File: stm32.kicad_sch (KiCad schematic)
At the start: 9 parts, among them CN2 XY308-2.54-4P, CN3 SM04B-SRSS-TB (LF)(SN), CN4 SM04B-SRSS-TB (LF)(SN), U1 STM32G431CBT6, U2 DRV8323SRTAR, U3 TMC2209-LA-T, U4 DRV8876PWPR, U6 HB-PH9-12727PB2GOB, U8 XY308-2.54-2P

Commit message: WIP
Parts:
- added C38, C49: CL10A475KO8NNNC, easyeda2kicad:C0603, symbol easyeda2kicad:CL10A475KO8NNNC
- added C39, C40, C41, C46, C47, C50, C51, C52, C53: CC0603KRX7R9BB104, easyeda2kicad:C0603, symbol easyeda2kicad:CC0603KRX7R9BB104
- added C42, C43, C48: CL10A105KB8NNNC, easyeda2kicad:C0603, symbol easyeda2kicad:CL10A105KB8NNNC
- added C44, C45: 0603CG7R0C500NT, easyeda2kicad:C0603, symbol easyeda2kicad:0603CG7R0C500NT
- added R20, R34, R40: 0603WAF4701T5E, easyeda2kicad:R0603, symbol easyeda2kicad:0603WAF4701T5E
- added R21, R30, R31: 0603WAF1002T5E, easyeda2kicad:R0603, symbol easyeda2kicad:0603WAF1002T5E
- added R28, R29: 0603WAF0000T5E, easyeda2kicad:R0603, symbol easyeda2kicad:0603WAF0000T5E
- added R41: 0603WAF1001T5E, easyeda2kicad:R0603, symbol easyeda2kicad:0603WAF1001T5E
- added R42: 0603WAF1000T5E, easyeda2kicad:R0603, symbol easyeda2kicad:0603WAF1000T5E
- added SW2: 6.0*6.0*6.0, easyeda2kicad:SW-SMD_4P-L6.0-W6.0-P4.50-LS8.6, symbol easyeda2kicad:6.0*6.0*6.0
- added X1: SC-32S32.768kHz20PPM7pF, easyeda2kicad:OSC-SMD_L3.2-W1.5, symbol easyeda2kicad:SC-32S32.768kHz20PPM7pF
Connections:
- net +3V3: now reaches U1.1 (VBAT)
- net +3V3: now also U1.20 (VREF+), U1.21 (VDDA), U1.24 (VDD), U1.36 (VDD), U1.48 (VDD), U3.15 (VCC_IO), U6.3, C38.1, C39.1, C40.1, C41.1, C42.1, C43.1, C46.1, C47.1, C48.1, C50.1, R20.1, R30.2, R31.2, R34.1, R40.1
- net GND: now reaches U1.19 (VSSA)
- net GND: now also U1.23 (VSS), U1.35 (VSS), U1.47 (VSS), U3.18 (GND), U3.20 (STDBY), U3.29 (EP), U3.3 (GND), U6.5, U6.7, C38.2, C39.2, C40.2, C41.2, C42.2, C43.2, C44.1, C45.1, C46.2, C47.2, C48.2, C49.2, C50.2, C51.2, C52.2, R21.1, R42.2, SW2.3, SW2.4
- net at U1.3 (PC14-OSC32_IN): now also R28.2
- net SWDIO: now reaches U1.37 (PA13)
- net SWDIO: now also U6.4, R40.2
- net SWCLK: now reaches U1.38 (PA14)
- net SWCLK: now also U6.6, R34.2
- net at U1.4 (PC15-OSC32_OUT): now also R29.2
- net BOOT0: now reaches U1.45 (PB8-BOOT0)
- net BOOT0: now also R20.2, R21.2
- net STM32_NRST: now reaches U1.7 (PG10-NRST)
- net STM32_NRST: now also R30.1, SW2.1, SW2.2
- net at U6.11: now also R42.1
- net VCP_RX: now reaches U6.13
- net VCP_TX: now reaches U6.14
- net UART_PDN_RX: now reaches U3.14 (PDN_UART)
- net UART_PDN_RX: now also R41.2
- net STEPPER_EN: now reaches U3.2 (ENN)
- net STEPPER_EN: now also R31.1
- net +VBAT: now reaches U3.22 (VS)
- net +VBAT: now also U3.28 (VS), C51.1, C52.1, C53.1
- net at U3.6 (VCP): now also C53.2
- net at U3.8 (5VOUT): now also C49.1
- new net OSC32_IN: C44.2, R28.1, X1.1
- new net OSC32_OUT: C45.2, R29.1, X1.2
- new net UART_PDN_TX: R41.1
- no-connect marks 5 -> 7
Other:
- note added: "ENN: enable=0 disable=1"
- note added: "JTAG/SW CONN"
- note added: "Original part number for the stm32 v3 set is : FTSH-107-01-L-DV-K-A"
- note added: "PB_SWITCH"
- note added: "VBAT"
- note added: "VDD"
- note added: "VDDA"
- note added: "VREF"
- moved on the sheet: CN2, U2, U3, U4, U8

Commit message: stepper and dc motors and stm32 config pins are ready
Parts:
- removed C42, C43, C48: CL10A105KB8NNNC, easyeda2kicad:C0603, symbol easyeda2kicad:CL10A105KB8NNNC
- removed C44, C45: 0603CG7R0C500NT, easyeda2kicad:C0603, symbol easyeda2kicad:0603CG7R0C500NT
- removed R20: 0603WAF4701T5E, easyeda2kicad:R0603, symbol easyeda2kicad:0603WAF4701T5E
- removed R28, R29: 0603WAF0000T5E, easyeda2kicad:R0603, symbol easyeda2kicad:0603WAF0000T5E
- removed X1: SC-32S32.768kHz20PPM7pF, easyeda2kicad:OSC-SMD_L3.2-W1.5, symbol easyeda2kicad:SC-32S32.768kHz20PPM7pF
- added C1, C10, C2, C3, C4: CL10B105KA8NNNC, easyeda2kicad:C0603, symbol easyeda2kicad:CL10B105KA8NNNC
- added C54, C55: CC0603KRX7R9BB104, easyeda2kicad:C0603, symbol easyeda2kicad:CC0603KRX7R9BB104
- added C56: ~, easyeda2kicad:C0603, symbol easyeda2kicad:CC0603KRX7R9BB104
- added C9: CL21A226MAYNNNE, easyeda2kicad:C0805, symbol easyeda_symbole:CL21A226MAYNNNE
- added D10, D11, D12: KT-0603R, easyeda2kicad:LED0603-RD, symbol easyeda2kicad:KT-0603R
- added D3: 0603 Green 509-620mcd, easyeda2kicad:LED0603-RD, symbol easyeda2kicad:0603Green509-620mcd
- added R22: ~, easyeda2kicad:R0603, symbol easyeda2kicad:0603WAF1002T5E
- added R23, R24, R25, R26: 0603WAF1000T5E, easyeda2kicad:R0603, symbol easyeda2kicad:0603WAF1000T5E
- added R32: 0603WAF1002T5E, easyeda2kicad:R0603, symbol easyeda2kicad:0603WAF1002T5E
- added R4, R6: 0603WAF1003T5E, easyeda2kicad:R0603, symbol easyeda2kicad:0603WAF1003T5E
- added R5: 0603WAF0000T5E, easyeda2kicad:R0603, symbol easyeda2kicad:0603WAF0000T5E
- added SW3: 6.0*6.0*6.0, easyeda2kicad:SW-SMD_4P-L6.0-W6.0-P4.50-LS8.6, symbol easyeda2kicad:6.0*6.0*6.0
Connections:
- net +3V3: now also U4.5 (VREF), C2.1, C3.1, C4.1, R26.1, R32.2
- net +VBAT: now also U4.11 (VM), C1.1, C10.1, C54.1, C55.2
- net GND: now also U3.2 (ENN), U3.23 (BRA), U3.25 (UNUSED), U3.27 (BRB), U4.15 (GND), U4.16 (PMODE), U4.17 (EP), U4.6 (IPROPI), U4.7 (IMODE), U4.9 (PGND), C1.2, C10.2, C2.2, C3.2, C4.2, C54.2, D10.1 (K), D11.1 (K), D3.1 (K), R22.1, R4.1, R5.2, SW3.3, SW3.4; no longer U3.20 (STDBY)
- net UART_PDN_RX: now also R22.2
- net at C49.1, U3.8 (5VOUT): now also R6.2
- net at U8.1: now also U4.8 (OUT1)
- net at U8.2: now also U4.10 (OUT2)
- net OSC_IN: now reaches U1.5 (PF0-OSC_IN)
- net OSC_OUT: now reaches U1.6 (PF1-OSC_OUT)
- net STEPPER_DIAG: now reaches U3.11 (DIAG)
- net STEPPER_DIAG: now also R25.2
- net at U3.13 (CLK): now also R5.1
- net STEPPER_STEP: now reaches U3.16 (STEP)
- net at U3.17 (VREF): now also R6.1
- net STEPPER_DIR: now reaches U3.19 (DIR)
- net at U3.4 (CPO): now also C9.1
- net at U3.5 (CPI): now also C9.2
- net DC_MOTOR_PWM_EN: now reaches U4.1 (EN/IN1)
- net at U4.12 (VCP): now also C55.1
- net at U4.13 (CPH): now also C56.2
- net at U4.14 (CPL): now also C56.1
- net DC_MOTOR_DIR: now reaches U4.2 (PH/IN2)
- net DC_MOTOR_SLEEP: now reaches U4.3 (nSLEEP)
- net LED_FAULT: now reaches U4.4 (nFAULT)
- net LED_FAULT: now also R31.1, D12.1 (K)
- net MOTOR_A1 renamed STEPPER_A1
- net MOTOR_A2 renamed STEPPER_A2
- net MOTOR_B1 renamed STEPPER_B1
- net MOTOR_B2 renamed STEPPER_B2
- removed net STEPPER_EN: R31.1, U3.2 (ENN)
- new net: D12.2 (A), R26.2
- new net: D3.2 (A), R23.1
- new net: D10.2 (A), R24.1
- new net: D11.2 (A), R25.1
- new net LED1: R23.2
- new net LED2: R24.2
- new net PB_SW1: R32.1, SW3.1, SW3.2
- new net STEPPER_STDBY: R4.2, U3.20 (STDBY)
- no-connect marks 7 -> 11
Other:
- note added: "I2C"
- note added: "LEDS"
- note added: "SPI"
- moved on the sheet: C38, C39, C40, C41, C46, C47, C49, CN3, R21, R34, R40, R41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

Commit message: bldc connections and stm32 io connection and adjustments
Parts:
- removed D10: KT-0603R, easyeda2kicad:LED0603-RD, symbol easyeda2kicad:KT-0603R
- removed R24: 0603WAF1000T5E, easyeda2kicad:R0603, symbol easyeda2kicad:0603WAF1000T5E
- added C12, C15: CL10B105KA8NNNC, easyeda2kicad:C0603, symbol easyeda2kicad:CL10B105KA8NNNC
- added C13, C14: ~, easyeda2kicad:C0603, symbol easyeda2kicad:CL10B105KA8NNNC
- added C59, C60: CC0603KRX7R9BB104, easyeda2kicad:C0603, symbol easyeda2kicad:CC0603KRX7R9BB104
- added D13: KT-0603R, easyeda2kicad:LED0603-RD, symbol easyeda2kicad:KT-0603R
- added R13, R16, R33, R35: 0603WAF1002T5E, easyeda2kicad:R0603, symbol easyeda2kicad:0603WAF1002T5E
- added R27: 0603WAF1000T5E, easyeda2kicad:R0603, symbol easyeda2kicad:0603WAF1000T5E
- added R28: 0603WAF220JT5E, easyeda2kicad:R0603, symbol easyeda2kicad:0603WAF220JT5E
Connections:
- net +3V3: now also CN4.2, U2.24 (VREF), C60.1, R13.2, R16.2, R27.1, R33.2, R35.2
- net +VBAT: now also U2.4 (VM), U2.5 (VDRAIN), C12.2, C13.2, C59.1
- net DC_MOTOR_DIR: now also U1.43 (PB6)
- net DC_MOTOR_PWM_EN: now also U1.31 (PA9)
- net DC_MOTOR_SLEEP: now also U1.2 (PC13)
- net GND: now also CN4.1, U2.32 (AGND), U2.40 (PGND), U2.41 (EP), C13.1, C15.1, C59.2, C60.2
- net LED1: now also U1.4 (PC15-OSC32_OUT)
- net PB_SW1: now also U1.3 (PC14-OSC32_IN)
- net STEPPER_DIR: now also U1.33 (PA11)
- net STEPPER_STDBY: now also U1.34 (PA12)
- net STEPPER_STEP: now also U1.32 (PA10)
- net VCP_RX: now also U1.11 (PA3)
- net VCP_TX: now also U1.10 (PA2)
- net BLDC_SPI_CS: now reaches U1.12 (PA4)
- net BLDC_SPI_CS: now also U2.29 (nSCS)
- net BLDC_SPI_SCK: now reaches U1.13 (PA5)
- net BLDC_SPI_SCK: now also U2.28 (SCLK)
- net BLDC_SPI_MISO: now reaches U1.14 (PA6)
- net BLDC_SPI_MISO: now also U2.26 (SDO), R33.1
- net BLDC_SPI_MOSI: now reaches U1.15 (PA7)
- net BLDC_SPI_MOSI: now also U2.27 (SDI)
- net VSENSE_C: now reaches U1.16 (PB0)
- net VSENSE_B: now reaches U1.17 (PB1)
- net VSENSE_A: now reaches U1.18 (PB2)
- net BLDC_STOP: now reaches U1.22 (PB10)
- net BLDC_STOP: now also U2.30 (ENABLE), U2.35 (INLA), U2.37 (INLB), U2.39 (INLC)
- net BLDC_SOC: now reaches U1.25 (PB11)
- net BLDC_SOC: now also U2.21 (SOC)
- net SPI2_CS: now reaches U1.26 (PB12)
- net SPI2_CS: now also CN3.1
- net SPI2_SCK: now reaches U1.27 (PB13)
- net SPI2_SCK: now also CN3.2
- net SPI2_MISO: now reaches U1.28 (PB14)
- net SPI2_MISO: now also CN3.3
- net SPI2_MOSI: now reaches U1.29 (PB15)
- net SPI2_MOSI: now also CN3.4
- net I2C3_SCL_R: now reaches U1.30 (PA8)
- net I2C3_SCL_R: now also R28.1
- net BLDC_INHC: now reaches U1.39 (PA15)
- net BLDC_INHC: now also U2.38 (INHC)
- net BLDC_INHB: now reaches U1.40 (PB3)
- net BLDC_INHB: now also U2.36 (INHB)
- net BLDC_INHA: now reaches U1.41 (PB4)
- net BLDC_INHA: now also U2.34 (INHA)
- net I2C3_SDA: now reaches U1.42 (PB5)
- net I2C3_SDA: now also CN4.3, R13.1
- net BLDC_SOA: now reaches U1.8 (PA0)
- net BLDC_SOA: now also U2.23 (SOA)
- net BLDC_SOB: now reaches U1.9 (PA1)
- net BLDC_SOB: now also U2.22 (SOB)
- net at U2.1 (CPL): now also C14.2
- net SNA: now reaches U2.10 (SNA)
- net SNB: now reaches U2.11 (SNB)
- net SPB: now reaches U2.12 (SPB)
- net GLB: now reaches U2.13 (GLB)
- net SHB: now reaches U2.14 (SHB)
- net GHB: now reaches U2.15 (GHB)
- net GHC: now reaches U2.16 (GHC)
- net SHC: now reaches U2.17 (SHC)
- net GLC: now reaches U2.18 (GLC)
- net SPC: now reaches U2.19 (SPC)
- net at U2.2 (CPH): now also C14.1
- net SNC: now reaches U2.20 (SNC)
- net BLDC_LED_FAULT: now reaches U2.25 (nFAULT)
- net BLDC_LED_FAULT: now also D13.1 (K), R35.1
- net at U2.3 (VCP): now also C12.1
- net 3V3_OUT: now reaches U2.33 (DVDD)
- net 3V3_OUT: now also C15.2
- net GHA: now reaches U2.6 (GHA)
- net SHA: now reaches U2.7 (SHA)
- net GLA: now reaches U2.8 (GLA)
- net SPA: now reaches U2.9 (SPA)
- net I2C3_SCL: now reaches CN4.4
- net I2C3_SCL: now also R16.1, R28.2
- net LED_FAULT renamed DC_MOTOR_LED_FAULT
- new net: D13.2 (A), R27.2
- no-connect marks 11 -> 15
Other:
- note added: "STM32G4"
- note removed: "stm32g4"
- moved on the sheet: C2, C3, C38, C39, C4, C40, C41, C46, C47, CN4, D12, D3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

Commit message: connection updates after lampel review
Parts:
- removed C9: CL21A226MAYNNNE, easyeda2kicad:C0805, symbol easyeda_symbole:CL21A226MAYNNNE
- removed R22: ~, easyeda2kicad:R0603, symbol easyeda2kicad:0603WAF1002T5E
- removed R31: 0603WAF1002T5E, easyeda2kicad:R0603, symbol easyeda2kicad:0603WAF1002T5E
- removed R4: 0603WAF1003T5E, easyeda2kicad:R0603, symbol easyeda2kicad:0603WAF1003T5E
- removed R5: 0603WAF0000T5E, easyeda2kicad:R0603, symbol easyeda2kicad:0603WAF0000T5E
- added C57: ~, easyeda2kicad:C0603, symbol easyeda2kicad:CC0603KRX7R9BB104
- added R36: 0603WAF1002T5E, easyeda2kicad:R0603, symbol easyeda2kicad:0603WAF1002T5E
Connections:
- net +3V3: now also R36.2
- net BLDC_LED_FAULT: now also U1.44 (PB7)
- net GND: now also U3.13 (CLK), U3.9 (MS1_AD0)
- net at U3.4 (CPO): now also C57.2
- net at U3.5 (CPI): now also C57.1
- net at U3.10 (MS2_AD1): now also R36.1
- no-connect marks 15 -> 13
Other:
- moved on the sheet: D11, D13, R25, R27, R41

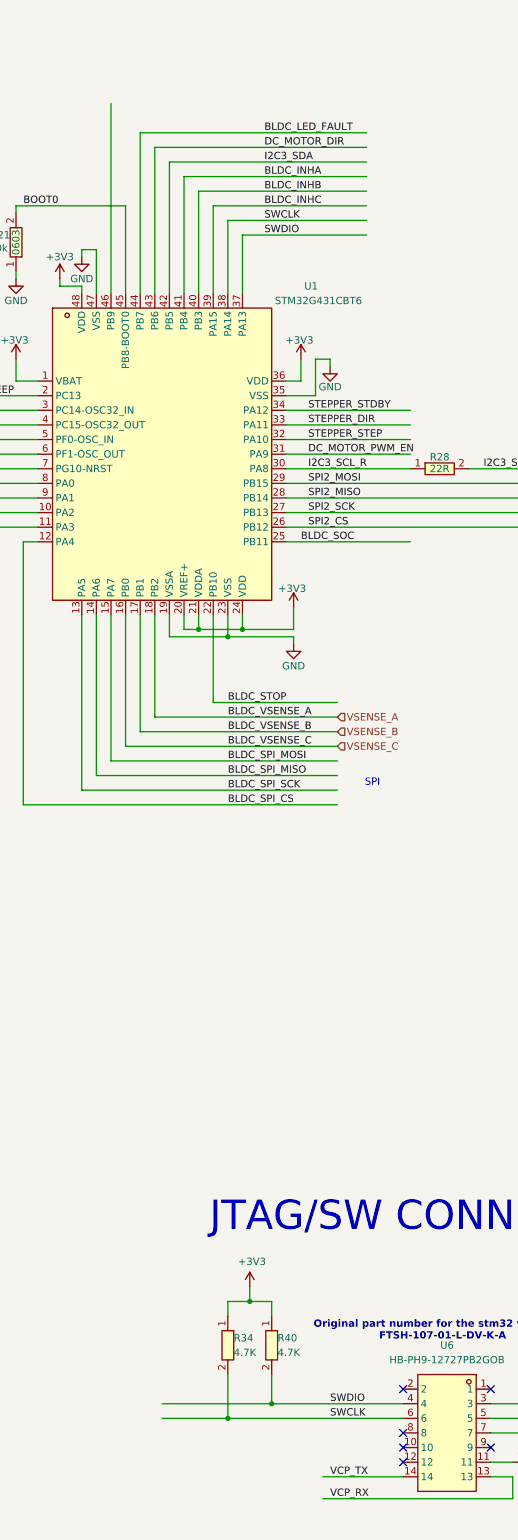
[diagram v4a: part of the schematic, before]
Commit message: adding SWO pin
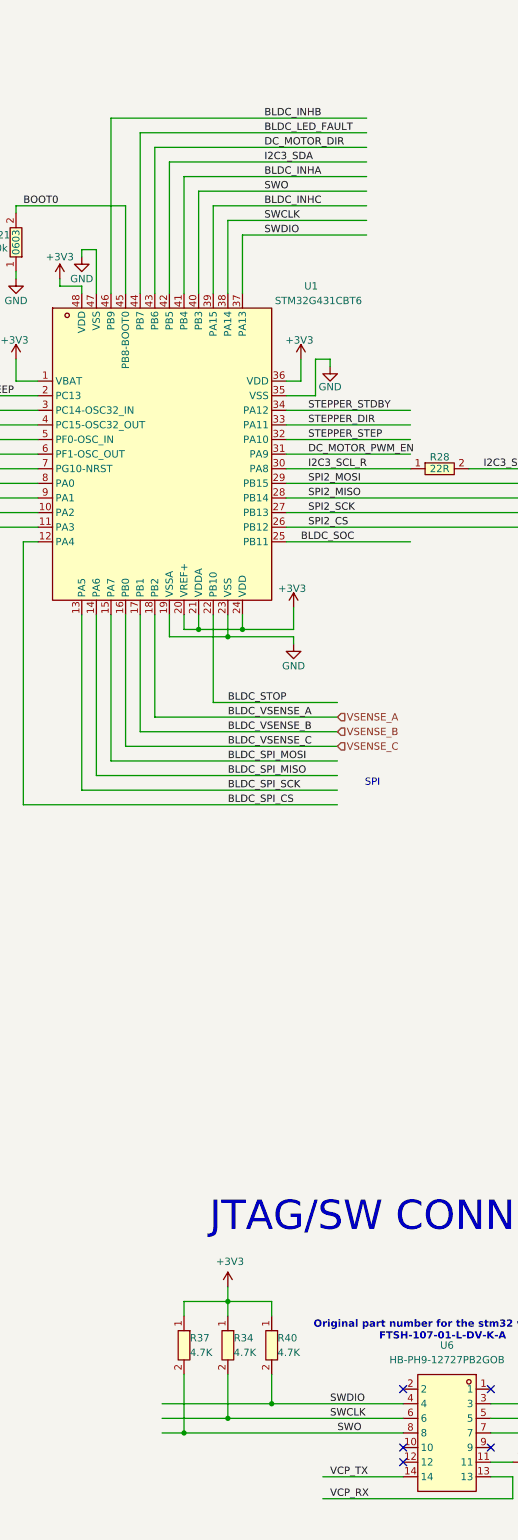
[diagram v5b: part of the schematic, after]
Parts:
- added R37: 0603WAF4701T5E, easyeda2kicad:R0603, symbol easyeda2kicad:0603WAF4701T5E
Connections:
- net +3V3: now also R37.1
- net BLDC_INHB: now also U1.46 (PB9); no longer U1.40 (PB3)
- net SWO: now reaches U6.8
- net SWO: now also U1.40 (PB3), R37.2
- no-connect marks 13 -> 12
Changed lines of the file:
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@@
 	)
 	(junction
+		(at 173.99 306.07)
+		(diameter 0)
+		(color 0 0 0 0)
+	)
+	(junction
 		(at 173.99 326.39)
 		(diameter 0)
@@
 	)
 	(junction
-		(at 177.8 306.07)
-		(diameter 0)
-		(color 0 0 0 0)
-	)
-	(junction
 		(at 502.92 52.07)
 		(diameter 0)
@@
 	)
 	(junction
+		(at 166.37 328.93)
+		(diameter 0)
+		(color 0 0 0 0)
+	)
+	(junction
 		(at 48.26 92.71)
 		(diameter 0)
@@
 	)
 	(no_connect
-		(at 204.47 328.93)
-	)
-	(no_connect
 		(at 204.47 321.31)
 	)
@@
 	(wire
 		(pts
+			(xy 166.37 318.77) (xy 166.37 328.93)
+		)
+		(stroke
+			(width 0)
+			(type default)
+		)
+	)
+	(wire
+		(pts
 			(xy 184.15 151.13) (xy 205.74 151.13)
 		)
@@
 	(wire
 		(pts
+			(xy 153.67 100.33) (xy 198.12 100.33)
+		)
+		(stroke
+			(width 0)
+			(type default)
+		)
+	)
+	(wire
+		(pts
 			(xy 163.83 107.95) (xy 198.12 107.95)
 		)
@@
 	(wire
 		(pts
+			(xy 166.37 328.93) (xy 204.47 328.93)
+		)
+		(stroke
+			(width 0)
+			(type default)
+		)
+	)
+	(wire
+		(pts
 			(xy 501.65 162.56) (xy 492.76 162.56)
 		)
@@
 	(wire
 		(pts
-			(xy 153.67 97.79) (xy 153.67 130.81)
+			(xy 153.67 100.33) (xy 153.67 130.81)
 		)
 		(stroke
 			(width 0)
 			(type default)
-			(color 255 0 0 1)
 		)
 	)
@@
 	(wire
 		(pts
+			(xy 166.37 306.07) (xy 173.99 306.07)
+		)
+		(stroke
+			(width 0)
+			(type default)
+		)
+	)
+	(wire
+		(pts
 			(xy 118.11 171.45) (xy 140.97 171.45)
 		)
@@
 	(wire
 		(pts
+			(xy 166.37 308.61) (xy 166.37 306.07)
+		)
+		(stroke
+			(width 0)
+			(type default)
+		)
+	)
+	(wire
+		(pts
 			(xy 414.02 222.25) (xy 414.02 208.28)
 		)
@@
 	(wire
 		(pts
+			(xy 162.56 328.93) (xy 166.37 328.93)
+		)
+		(stroke
+			(width 0)
+			(type default)
+		)
+	)
+	(wire
+		(pts
 			(xy 184.15 168.91) (xy 267.97 168.91)
 		)
@@
 	(wire
 		(pts
-			(xy 181.61 306.07) (xy 177.8 306.07)
-		)
-		(stroke
-			(width 0)
-			(type default)
-		)
-	)
-	(wire
-		(pts
 			(xy 236.22 328.93) (xy 236.22 334.01)
 		)
@@
 	(wire
 		(pts
-			(xy 177.8 306.07) (xy 173.99 306.07)
+			(xy 173.99 306.07) (xy 181.61 306.07)
 		)
 		(stroke
@@
 	(wire
 		(pts
-			(xy 177.8 306.07) (xy 177.8 303.53)
+			(xy 173.99 306.07) (xy 173.99 303.53)
 		)
 		(stroke
@@
 		)
 	)
-	(label "BLDC_INHB"
-		(at 180.34 113.03 0)
-		(effects
-			(font
-				(size 1.27 1.27)
-			)
-			(justify left bottom)
-		)
-	)
 	(label "STEPPER_A2"
 		(at 500.38 72.39 0)
@@
 		)
 	)
+	(label "SWO"
+		(at 180.34 113.03 0)
+		(effects
+			(font
+				(size 1.27 1.27)
+			)
+			(justify left bottom)
+		)
+	)
 	(label "VCP_RX"
 		(at 191.77 340.36 0)
@@
 		)
 	)
+	(label "SWO"
+		(at 193.04 328.93 0)
+		(effects
+			(font
+				(size 1.27 1.27)
+			)
+			(justify left bottom)
+		)
+	)
 	(label "BLDC_SPI_MISO"
 		(at 438.15 205.74 0)
@@
 		)
 	)
+	(label "BLDC_INHB"
+		(at 180.34 100.33 0)
+		(effects
+			(font
+				(size 1.27 1.27)
+			)
+			(justify left bottom)
+		)
+	)
 	(label "I2C3_SCL"
 		(at 218.44 161.29 0)
@@
 	(symbol
 		(lib_id "SAMC21_breakout-rescue:+3V3-power")
-		(at 177.8 303.53 0)
+		(at 173.99 303.53 0)
 		(unit 1)
 		(exclude_from_sim no)
@@
 		(dnp no)
 		(property "Reference" "#PWR021"
-			(at 177.8 307.34 0)
+			(at 173.99 307.34 0)
 			(effects
 				(font
@@
 		)
 		(property "Value" "+3V3"
-			(at 178.181 299.1358 0)
+			(at 174.371 299.1358 0)
 			(effects
 				(font
@@
 		)
 		(property "Footprint" ""
-			(at 177.8 303.53 0)
+			(at 173.99 303.53 0)
 			(effects
 				(font
@@
 		)
 		(property "Datasheet" ""
-			(at 177.8 303.53 0)
+			(at 173.99 303.53 0)
 			(effects
 				(font
@@
 		)
 		(property "Description" ""
-			(at 177.8 303.53 0)
+			(at 173.99 303.53 0)
 			(effects
 				(font
@@
 					(unit 1)
 				)
+			)
+		)
+	)
+	(symbol
+		(lib_id "easyeda2kicad:0603WAF4701T5E")
+		(at 166.37 313.69 270)
+		(unit 1)
+		(exclude_from_sim no)
+		(in_bom yes)
+		(on_board yes)
+		(dnp no)
+		(property "Reference" "R37"
+			(at 167.386 312.42 90)
+			(effects
+				(font
+					(size 1.27 1.27)
+				)
+				(justify left)
+			)
+		)
+		(property "Value" "0603WAF4701T5E"
+			(at 161.29 313.69 0)
+			(effects
+				(font
+					(size 1.27 1.27)
+				)
+				(hide yes)
+			)
+		)
+		(property "Footprint" "easyeda2kicad:R0603"
+			(at 158.75 313.69 0)
+			(effects
+				(font
+					(size 1.27 1.27)
+				)
+				(hide yes)
+			)
+		)
+		(property "Datasheet" "https://lcsc.com/product-detail/Chip-Resistor-Surface-Mount-UniOhm_4-7KR-4701-1_C23162.html"
+			(at 156.21 313.69 0)
+			(effects
+				(font
+					(size 1.27 1.27)
+				)
+				(hide yes)
+			)
+		)
+		(property "Description" "4.7K"
+			(at 167.386 314.96 90)
+			(effects
+				(font
+					(size 1.27 1.27)
+				)
+				(justify left)
+			)
+		)
+		(property "LCSC Part" "C23162"
+			(at 153.67 313.69 0)
+			(effects
+				(font
+					(size 1.27 1.27)
+				)
+				(hide yes)
+			)
+		)
+		(pin "1"
+		)
+		(pin "2"
+		)
+		(instances
+			(project "stm32G4"
+				(path "/97277ecc-4d45-42d3-be9a-6b43805ad0c6/9223e125-7c28-4305-a4e4-f70e2a17a8a2"
+					(reference "R37")
+					(unit 1)
+				)

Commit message: Added swaps
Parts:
- added C11, C9: CL10C150JB8NNNC, easyeda2kicad:C0603, symbol easyeda_symbole:CL10C150JB8NNNC
- added R4: 0603WAF1001T5E, easyeda2kicad:R0603, symbol easyeda_symbole:0603WAF1001T5E
- added U5: ABM8-272-T3_C20625731, easyeda2kicad:CRYSTAL-SMD_4P-L3.2-W2.5-BL, symbol easyeda_symbole:ABM8-272-T3_C20625731
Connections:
- net BLDC_INHA: now also U1.30 (PA8); no longer U1.41 (PB4)
- net BLDC_INHB: now also U1.31 (PA9); no longer U1.46 (PB9)
- net BLDC_INHC: now also U1.32 (PA10); no longer U1.39 (PA15)
- net BLDC_LED_FAULT: now also U1.17 (PB1); no longer U1.44 (PB7)
- net BLDC_SOA: now also U1.10 (PA2); no longer U1.8 (PA0)
- net BLDC_SOB: now also U1.12 (PA4); no longer U1.9 (PA1)
- net BLDC_SOC: now also U1.11 (PA3); no longer U1.25 (PB11)
- net BLDC_SPI_CS: now also U1.16 (PB0); no longer U1.12 (PA4)
- net BLDC_STOP: now also U1.34 (PA12); no longer U1.22 (PB10)
- net DC_MOTOR_DIR: now also U1.2 (PC13); no longer U1.43 (PB6)
- net DC_MOTOR_PWM_EN: now also U1.42 (PB5); no longer U1.31 (PA9)
- net DC_MOTOR_SLEEP: now also U1.26 (PB12); no longer U1.2 (PC13)
- net GND: now also C11.2, C9.1, U5.2 (GND), U5.4 (GND)
- net I2C3_SCL: now also U1.39 (PA15)
- net I2C3_SCL_R: no longer R28.1, U1.30 (PA8)
- net I2C3_SDA: now also U1.46 (PB9); no longer U1.42 (PB5)
- net OSC_IN: now also C9.2, U5.1
- net OSC_OUT: now also R4.2
- net SPI2_CS: now also U1.22 (PB10); no longer U1.26 (PB12)
- net STEPPER_DIR: now also U1.18 (PB2); no longer U1.33 (PA11)
- net STEPPER_STDBY: now also U1.41 (PB4); no longer U1.34 (PA12)
- net STEPPER_STEP: now also U1.33 (PA11); no longer U1.32 (PA10)
- net UART_PDN_RX: now also U1.43 (PB6)
- net UART_PDN_TX: now also U1.44 (PB7)
- net VCP_RX: no longer U1.11 (PA3)
- net VCP_TX: no longer U1.10 (PA2)
- net VSENSE_A: now also U1.8 (PA0); no longer U1.18 (PB2)
- net VSENSE_B: now also U1.9 (PA1); no longer U1.17 (PB1)
- net VSENSE_C: now also U1.25 (PB11); no longer U1.16 (PB0)
- new net: C11.1, R4.1, U5.3
